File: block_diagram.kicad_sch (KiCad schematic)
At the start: 0 parts

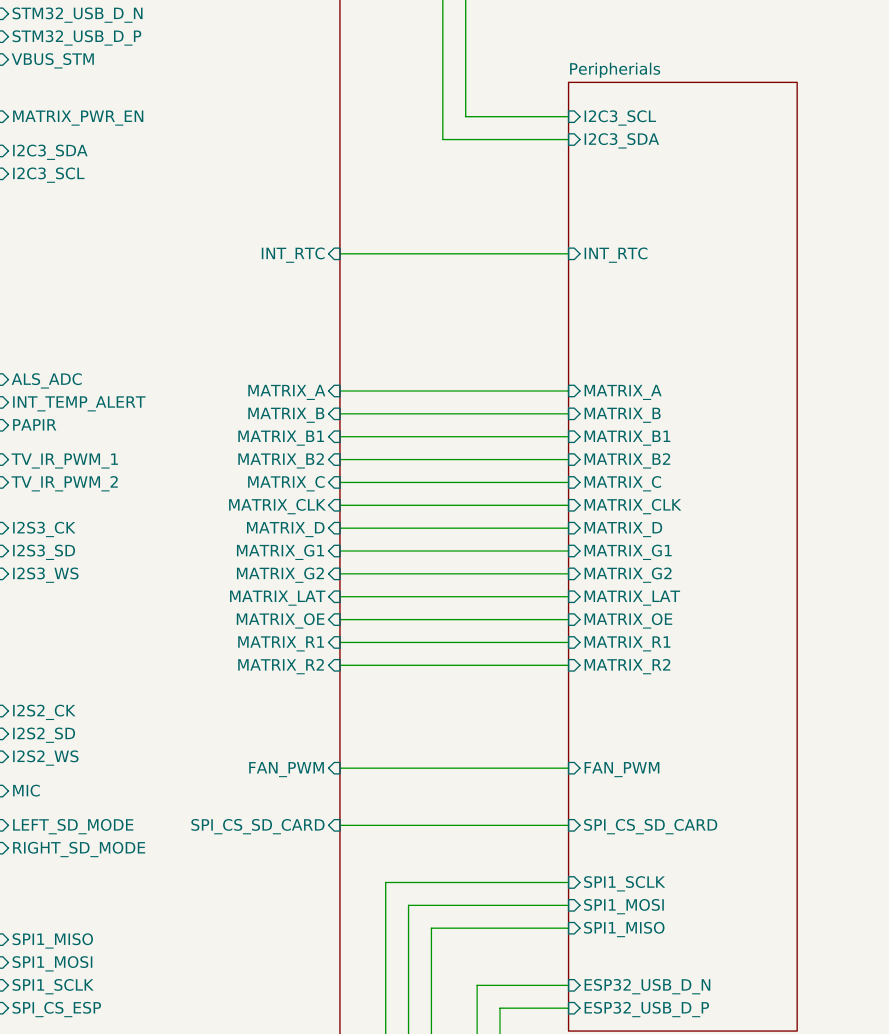
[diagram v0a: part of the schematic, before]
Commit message: mounting holes, hook up mini to stm32 g4
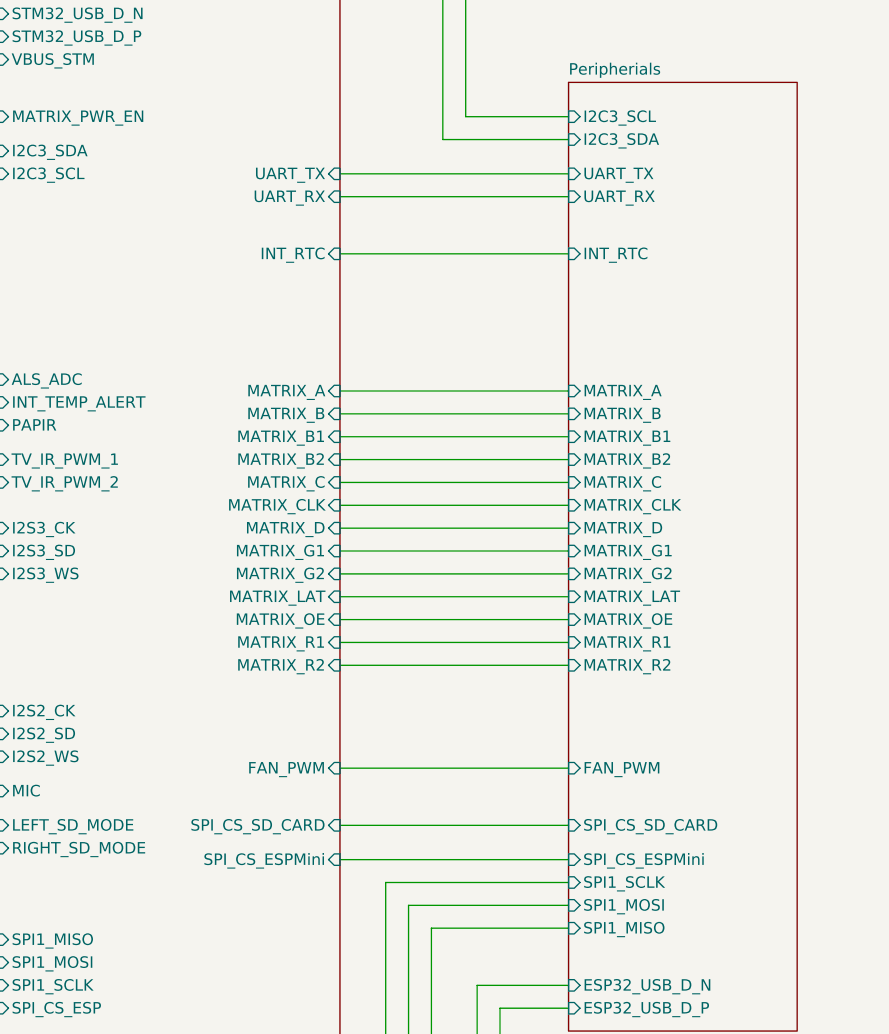
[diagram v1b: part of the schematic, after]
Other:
- sheet Peripherials ports: added SPI_CS_ESPMini, UART_RX, UART_TX; removed none
- sheet STM32G4 ports: added SPI_CS_ESPMini, UART_RX, UART_TX; removed none
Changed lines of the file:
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@@
+	(wire
+		(pts
+			(xy 140.97 135.89) (xy 166.37 135.89)
+		)
+		(stroke
+			(width 0)
+			(type default)
+		)
+	)
 	(wire
 		(pts
@@
 	(wire
 		(pts
+			(xy 140.97 59.69) (xy 166.37 59.69)
+		)
+		(stroke
+			(width 0)
+			(type default)
+		)
+	)
+	(wire
+		(pts
 			(xy 82.55 156.21) (xy 64.77 156.21)
 		)
@@
 		(pts
 			(xy 64.77 25.4) (xy 102.87 25.4)
+		)
+		(stroke
+			(width 0)
+			(type default)
+		)
+	)
+	(wire
+		(pts
+			(xy 140.97 62.23) (xy 166.37 62.23)
 		)
 		(stroke
@@
 			)
 		)
+		(pin "SPI_CS_ESPMini" input
+			(at 140.97 135.89 0)
+			(effects
+				(font
+					(size 1.27 1.27)
+				)
+				(justify right)
+			)
+		)
+		(pin "UART_RX" input
+			(at 140.97 62.23 0)
+			(effects
+				(font
+					(size 1.27 1.27)
+				)
+				(justify right)
+			)
+		)
+		(pin "UART_TX" input
+			(at 140.97 59.69 0)
+			(effects
+				(font
+					(size 1.27 1.27)
+				)
+				(justify right)
+			)
+		)
 		(instances
 			(project "SeniorDesign_PCB"
@@
 			(effects
 				(font
+					(size 1.27 1.27)
+				)
+				(justify left)
+			)
+		)
+		(pin "SPI_CS_ESPMini" input
+			(at 166.37 135.89 180)
+			(effects
+				(font
+					(size 1.27 1.27)
+				)
+				(justify left)
+			)
+		)
+		(pin "UART_RX" input
+			(at 166.37 62.23 180)
+			(effects
+				(font
+					(size 1.27 1.27)
+				)
+				(justify left)
+			)
+		)
+		(pin "UART_TX" input
+			(at 166.37 59.69 180)
+			(effects
+				(font

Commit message: pwr
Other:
- sheet Peripherials ports: added none; removed SPI_CS_ESPMini, UART_RX, UART_TX
- sheet STM32G4 ports: added none; removed SPI_CS_ESPMini, UART_RX, UART_TX
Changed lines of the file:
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@@
-	(wire
-		(pts
-			(xy 140.97 135.89) (xy 166.37 135.89)
-		)
-		(stroke
-			(width 0)
-			(type default)
-		)
-	)
 	(wire
 		(pts
@@
 	(wire
 		(pts
-			(xy 140.97 59.69) (xy 166.37 59.69)
-		)
-		(stroke
-			(width 0)
-			(type default)
-		)
-	)
-	(wire
-		(pts
 			(xy 82.55 156.21) (xy 64.77 156.21)
 		)
@@
 		(pts
 			(xy 64.77 25.4) (xy 102.87 25.4)
-		)
-		(stroke
-			(width 0)
-			(type default)
-		)
-	)
-	(wire
-		(pts
-			(xy 140.97 62.23) (xy 166.37 62.23)
 		)
 		(stroke
@@
 			)
 		)
-		(pin "SPI_CS_ESPMini" input
-			(at 140.97 135.89 0)
-			(effects
-				(font
-					(size 1.27 1.27)
-				)
-				(justify right)
-			)
-		)
-		(pin "UART_RX" input
-			(at 140.97 62.23 0)
-			(effects
-				(font
-					(size 1.27 1.27)
-				)
-				(justify right)
-			)
-		)
-		(pin "UART_TX" input
-			(at 140.97 59.69 0)
-			(effects
-				(font
-					(size 1.27 1.27)
-				)
-				(justify right)
-			)
-		)
 		(instances
 			(project "SeniorDesign_PCB"
@@
 			(effects
 				(font
-					(size 1.27 1.27)
-				)
-				(justify left)
-			)
-		)
-		(pin "SPI_CS_ESPMini" input
-			(at 166.37 135.89 180)
-			(effects
-				(font
-					(size 1.27 1.27)
-				)
-				(justify left)
-			)
-		)
-		(pin "UART_RX" input
-			(at 166.37 62.23 180)
-			(effects
-				(font
-					(size 1.27 1.27)
-				)
-				(justify left)
-			)
-		)
-		(pin "UART_TX" input
-			(at 166.37 59.69 180)
-			(effects
-				(font

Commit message: fixing again
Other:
- sheet Peripherials ports: added SPI_CS_ESPMini; removed none
- sheet STM32G4 ports: added SPI_CS_ESPMini; removed 5V_VOLTS
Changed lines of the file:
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@@
+	(wire
+		(pts
+			(xy 140.97 129.54) (xy 166.37 129.54)
+		)
+		(stroke
+			(width 0)
+			(type default)
+		)
+	)
 	(wire
 		(pts
@@
 			)
 		)
-		(pin "5V_VOLTS" input
-			(at 102.87 34.29 180)
-			(effects
-				(font
-					(size 1.27 1.27)
-				)
-				(justify left)
-			)
-		)
 		(pin "I_ANA" input
 			(at 102.87 31.75 180)
@@
 				)
 				(justify left)
+			)
+		)
+		(pin "SPI_CS_ESPMini" input
+			(at 140.97 129.54 0)
+			(effects
+				(font
+					(size 1.27 1.27)
+				)
+				(justify right)
 			)
 		)
@@
 			(effects
 				(font
+					(size 1.27 1.27)
+				)
+				(justify left)
+			)
+		)
+		(pin "SPI_CS_ESPMini" input
+			(at 166.37 129.54 180)
+			(effects
+				(font

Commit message: shunts
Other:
- sheet Power ports: added none; removed 5V_VOLTS
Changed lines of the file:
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@@
-	(wire
-		(pts
-			(xy 64.77 34.29) (xy 102.87 34.29)
-		)
-		(stroke
-			(width 0)
-			(type default)
-		)
-	)
 	(wire
 		(pts
@@
 			(effects
 				(font
-					(size 1.27 1.27)
-				)
-				(justify right)
-			)
-		)
-		(pin "5V_VOLTS" input
-			(at 64.77 34.29 0)
-			(effects
-				(font

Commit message: saving progress
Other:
- sheet Peripherials renamed Peripherals
- sheet Peripherals ports: added 5V_Buck; removed none
- sheet Power ports: added 5V_Buck; removed none
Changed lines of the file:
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@@
+	(wire
+		(pts
+			(xy 64.77 20.32) (xy 88.9 20.32)
+		)
+		(stroke
+			(width 0)
+			(type default)
+		)
+	)
 	(wire
 		(pts
@@
 	(wire
 		(pts
+			(xy 158.75 50.8) (xy 166.37 50.8)
+		)
+		(stroke
+			(width 0)
+			(type default)
+		)
+	)
+	(wire
+		(pts
 			(xy 140.97 83.82) (xy 166.37 83.82)
 		)
@@
 	(wire
 		(pts
+			(xy 158.75 12.7) (xy 158.75 50.8)
+		)
+		(stroke
+			(width 0)
+			(type default)
+		)
+	)
+	(wire
+		(pts
 			(xy 64.77 31.75) (xy 102.87 31.75)
 		)
@@
 	(wire
 		(pts
+			(xy 88.9 20.32) (xy 88.9 12.7)
+		)
+		(stroke
+			(width 0)
+			(type default)
+		)
+	)
+	(wire
+		(pts
 			(xy 64.77 59.69) (xy 82.55 59.69)
 		)
@@
 		(pts
 			(xy 64.77 101.6) (xy 102.87 101.6)
+		)
+		(stroke
+			(width 0)
+			(type default)
+		)
+	)
+	(wire
+		(pts
+			(xy 88.9 12.7) (xy 158.75 12.7)
 		)
 		(stroke
@@
 	)
 	(sheet
-		(at 39.37 21.59)
-		(size 25.4 40.64)
+		(at 39.37 16.51)
+		(size 25.4 45.72)
 		(exclude_from_sim no)
 		(in_bom yes)
@@
 		)
 		(property "Sheetname" "Power"
-			(at 39.37 20.8784 0)
+			(at 39.37 15.7984 0)
 			(show_name no)
 			(do_not_autoplace no)
@@
 			)
 		)
+		(pin "5V_Buck" input
+			(at 64.77 20.32 0)
+			(effects
+				(font
+					(size 1.27 1.27)
+				)
+				(justify right)
+			)
+		)
 		(instances
 			(project "SeniorDesign_PCB"
@@
 	)
 	(sheet
-		(at 166.37 49.53)
-		(size 25.4 105.41)
+		(at 166.37 46.99)
+		(size 25.4 107.95)
 		(exclude_from_sim no)
 		(in_bom yes)
@@
 			(color 0 0 0 0)
 		)
-		(property "Sheetname" "Peripherials"
-			(at 166.37 48.8184 0)
+		(property "Sheetname" "Peripherals"
+			(at 166.37 46.2784 0)
 			(show_name no)
 			(do_not_autoplace no)
@@
 		)
 		(property "Sheetfile" "Peripherials.kicad_sch"
-			(at 166.624 155.956 0)
+			(at 166.624 153.416 0)
 			(show_name no)
 			(do_not_autoplace no)
@@
 			(effects
 				(font
+					(size 1.27 1.27)
+				)
+				(justify left)
+			)
+		)
+		(pin "5V_Buck" input
+			(at 166.37 50.8 180)
+			(effects
+				(font

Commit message: Fixed
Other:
- sheet Peripherals ports: added MATRIX_PWR_EN; removed none
